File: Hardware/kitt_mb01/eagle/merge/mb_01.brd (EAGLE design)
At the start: 160 x 100 mm, 115 parts, among them CON1 ARDUINO_UNO, IC1.01 RT8293A, IC2.00 BQ24266RGET, IC3.01 LSM9DS1, P2 S2B-PH-K-S(LF)(SN), U1 MCP23017-E, U6.01 TPS61032RSARPSDO-G16, U7.01 SI1922EDH, X7.02 HEAD-LIGHT, X7.03 TAIL-LIGHT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

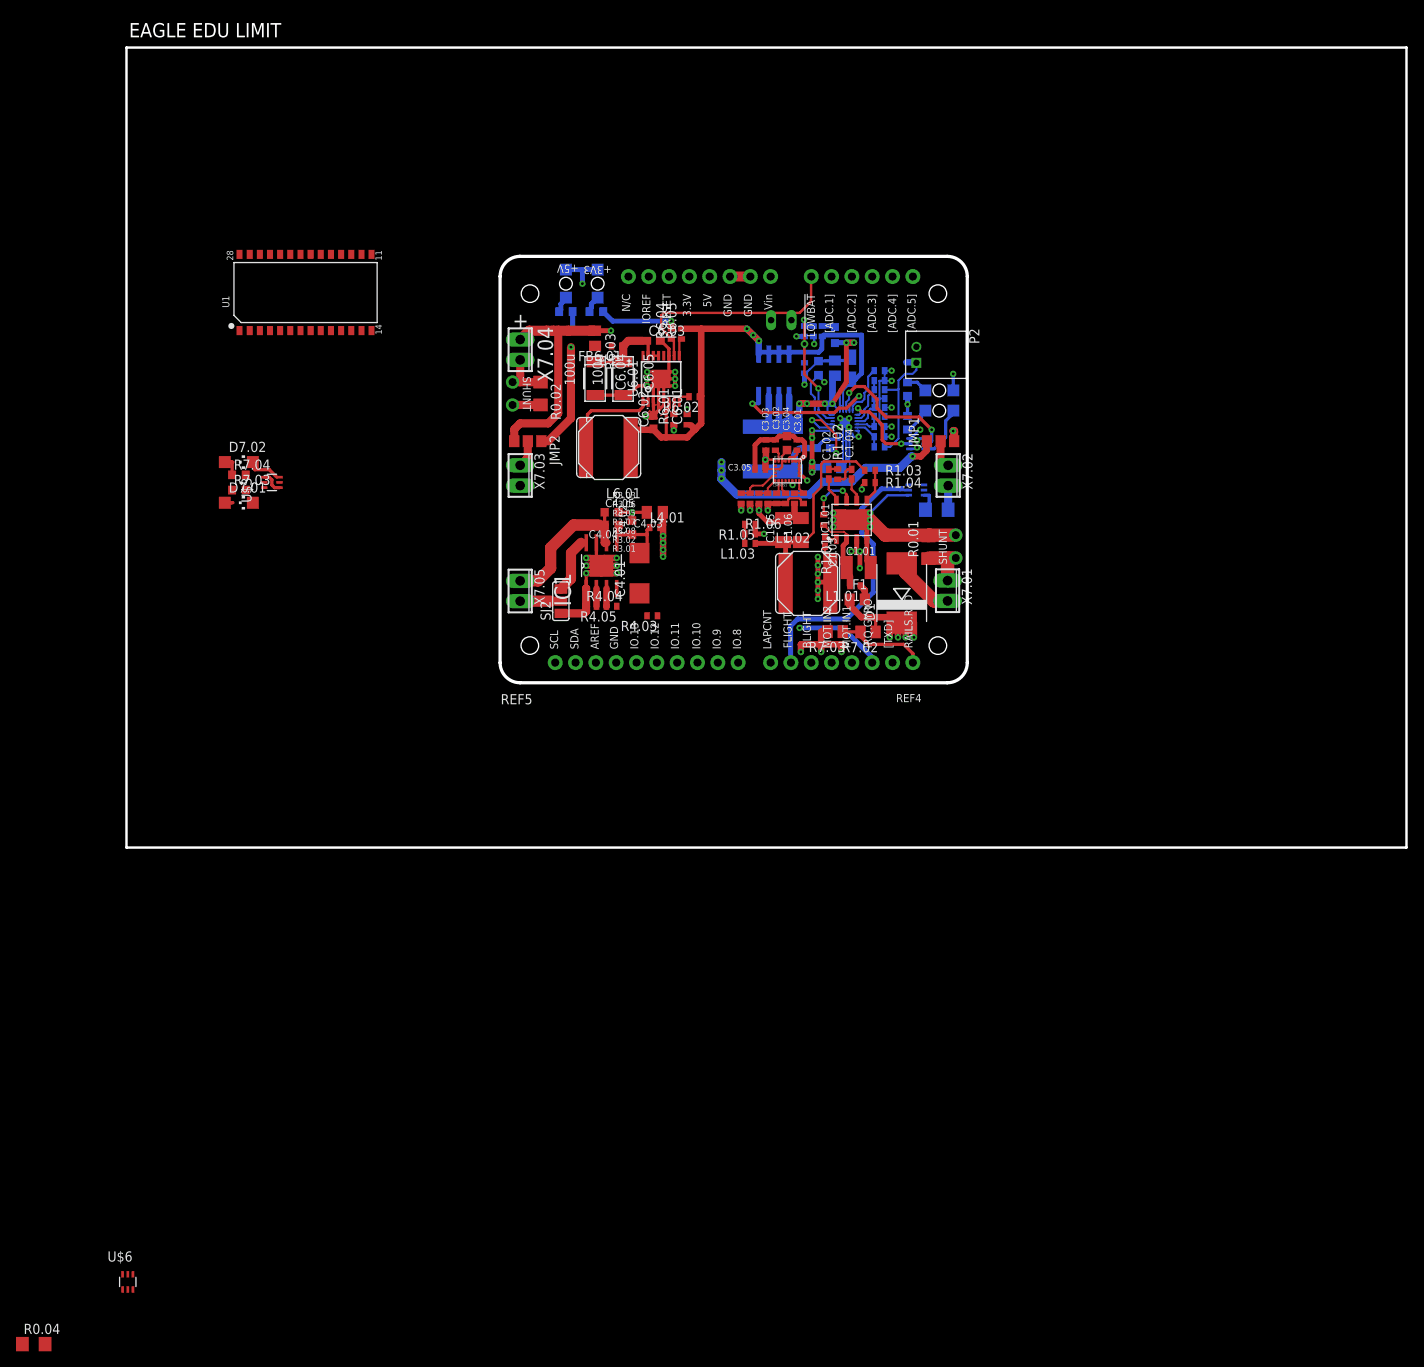
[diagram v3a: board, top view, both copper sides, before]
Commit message: snapshot of board merge : nearing it's "completion" edition
things to do:
-> either find a good placement for GP-indicators,
   or drop alltogether (what purpose?)
-> (re)move idea about port expander (DB01 maybe?)
-> add some fancy-pants logos, fiducial marks and layer count
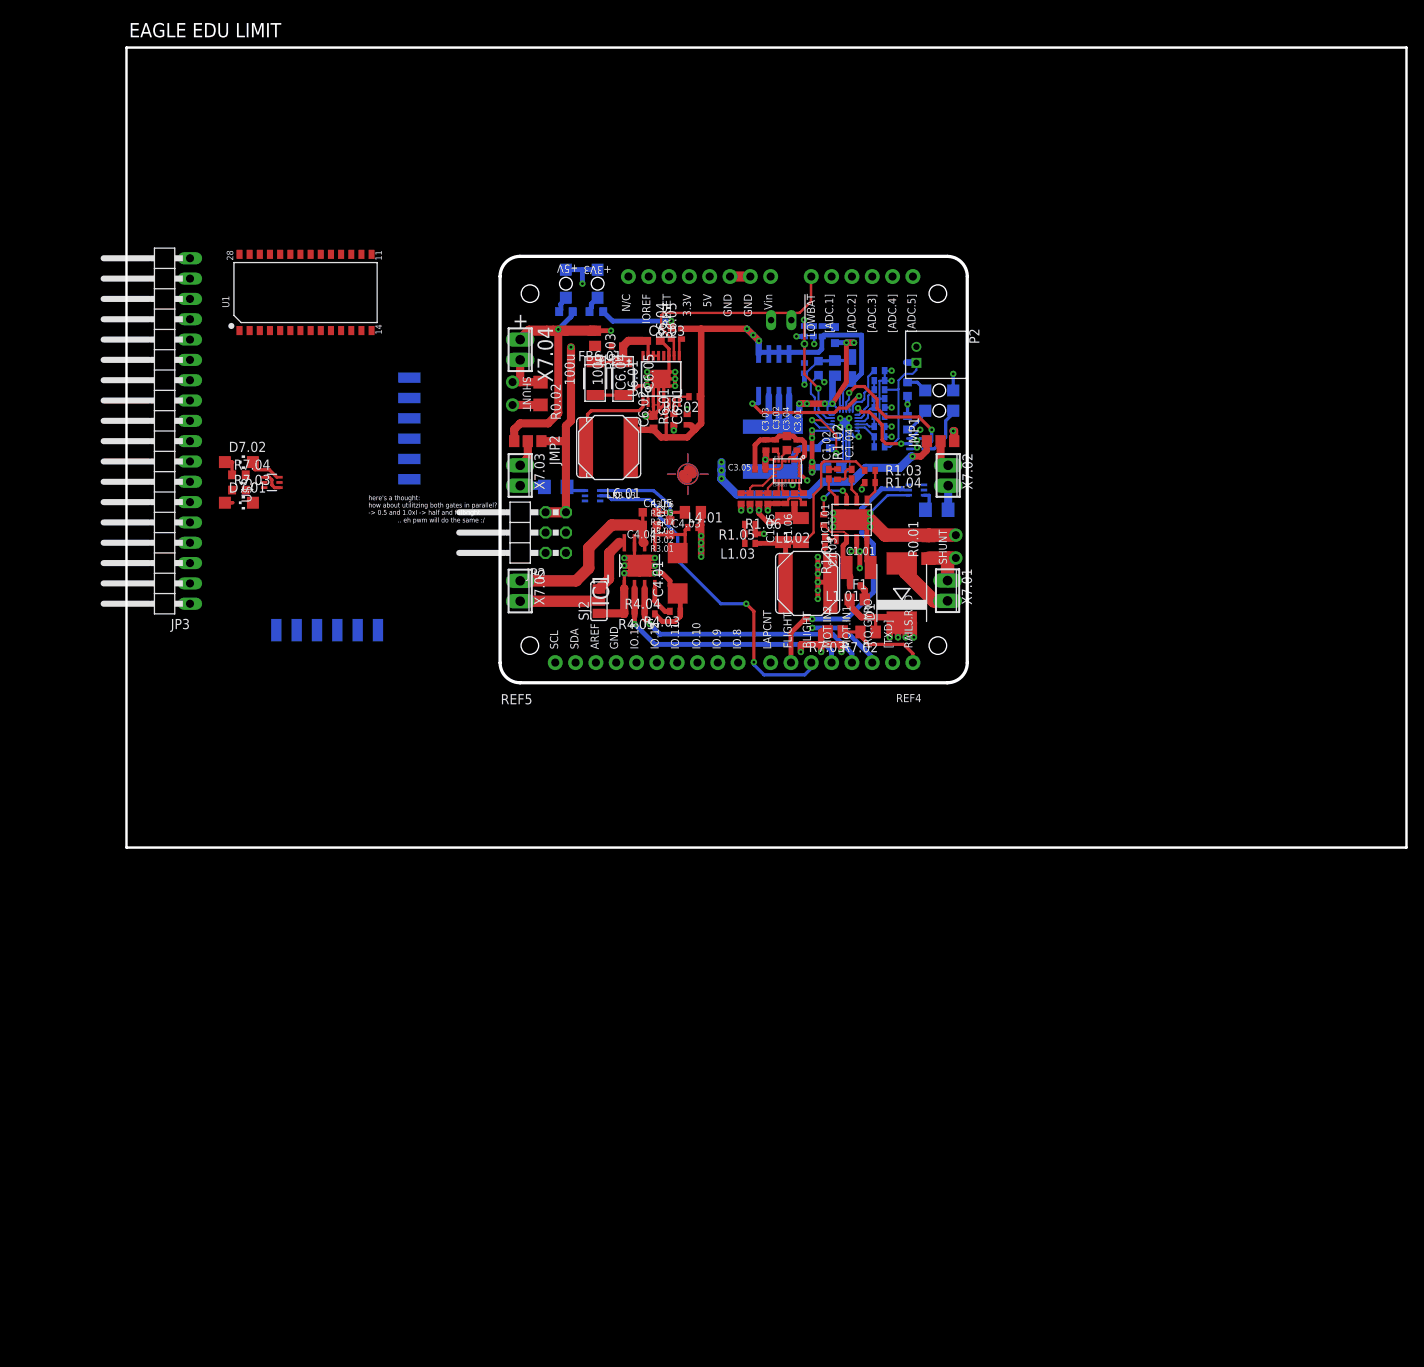
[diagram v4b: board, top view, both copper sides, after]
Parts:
- added J1, J2: CON_HEADER_1X06-SMD-RIGHT-ANGLED, dp_devices:M1X6_MALE_RIGHT_ANGLED_SMD
- added JP2: (no value), pinhead:2X03/90
- added JP3: (no value), pinhead:1X18/90
- added U$5: (no value), marks:PASS-ROUND
- moved R0.04 125.5 mm to (53.7, 45.1), flipped to the bottom
- moved U$6 114.2 mm to (58.3, 44.0), flipped to the bottom, turned to 90 degrees
- moved R4.04 4.86 mm to (62.9, 29.2)
- moved R4.05 4.86 mm to (65.4, 29.2)
- moved C4.04 4.76 mm to (65.4, 40.3)
- moved C4.05 4.76 mm to (65.4, 41.9)
- moved IC1 4.76 mm to (64.1, 35.2)
- moved SJ2 4.76 mm to (59.1, 30.8)
- moved C4.02 4.76 mm to (67.9, 40.0)
- moved C4.01 4.76 mm to (68.9, 34.3)
- moved C4.03 4.76 mm to (70.8, 41.9)
- moved L4.01 4.76 mm to (70.8, 40.0)
- moved R4.03 2.91 mm to (68.6, 29.5)
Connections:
- new net CAR.SPEED: CON1.IO.8, JP2.2
- net +3V3: now also JP2.5, JP2.6
- net CAR.BLIGHT: now also U$6.5
- net CAR.LAPCNT: now also JP2.1
- net GND: now also JP2.3, JP2.4
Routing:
- net CAR.BLIGHT: track 0.00 -> 43.0 mm, vias 0 -> 2
- net MOT.IN2: track 2.24 -> 33.8 mm, vias 0 -> 1
- net MOT.IN1: track 2.24 -> 33.6 mm, vias 0 -> 1
- net CAR.LAPCNT: track 0.00 -> 30.3 mm
- net CAR.SPEED: track 0.00 -> 29.5 mm
- net GND: track 221.4 -> 244.0 mm
- net +3V3: track 132.8 -> 145.5 mm
- net N$9: track 5.08 -> 9.84 mm
- net N$33: track 19.3 -> 24.1 mm
- net N$35: track 0.00 -> 4.00 mm
- net +12V: track 66.3 -> 62.3 mm
- net N$46: track 0.00 -> 3.09 mm
- net N$47: track 0.00 -> 2.42 mm
- net !IRQ_GYRO: track 37.2 -> 35.0 mm
- net +5V: track 139.3 -> 141.1 mm, vias 5 -> 6
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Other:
- board text added: ".. eh pwm will do the same :/"
- board text added: "here's a thought: how about utilitzing both gates in parallel? -> 0.5 and 1.0xI -> half and fulbright"

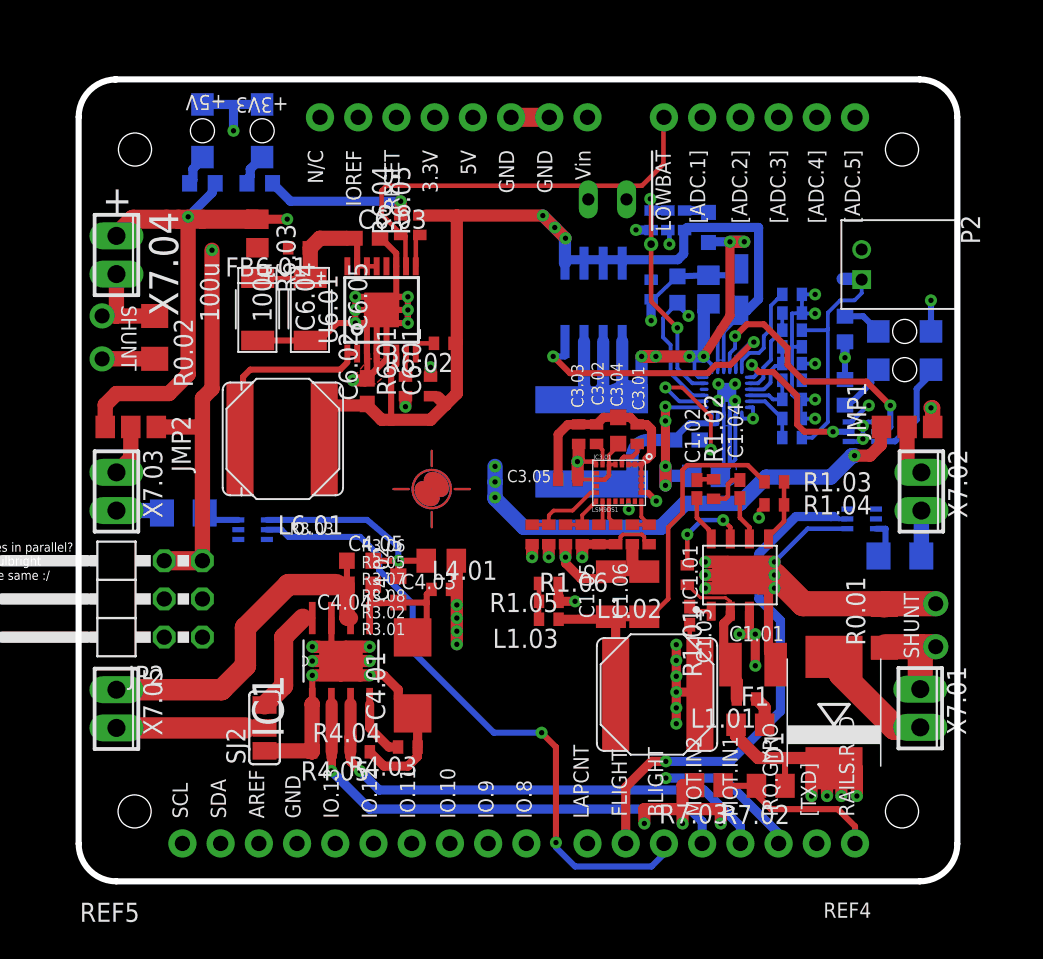
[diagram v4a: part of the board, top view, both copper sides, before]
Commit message: added layer reference onto board
for the record: it's binary, because it needs less space
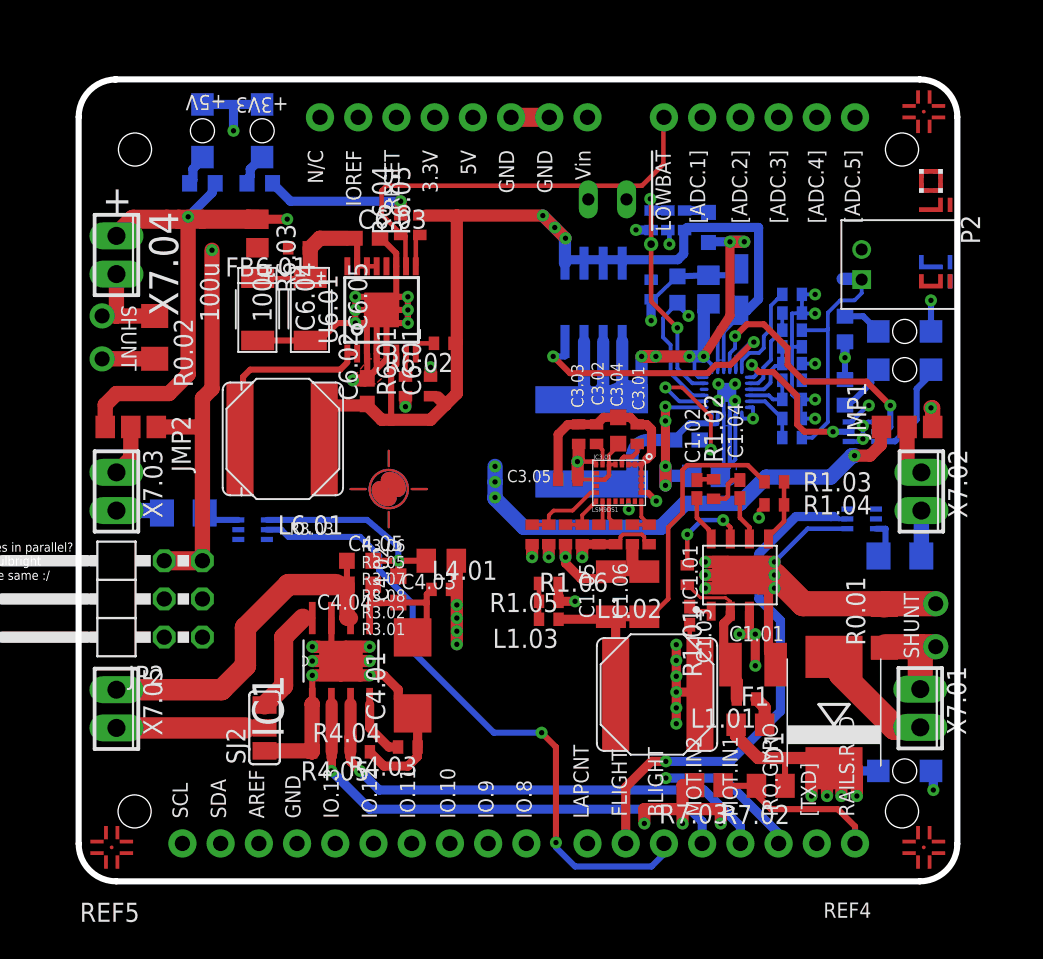
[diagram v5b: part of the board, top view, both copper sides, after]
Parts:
- added D7.07: OK+12V, led:CHIPLED_1206
- added R7,05: 330R, rcl:R0603
- added REF1: REF.LAYERS, kitt.refs:REF_LAYERS
- added U$7, U$8, U$9: (no value), marks:PASSER-CIRCLE
- moved U$5 2.86 mm to (67.3, 46.7)
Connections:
- new net N$44: D7.07.A, R7,05.1
- net +12V: now also R7,05.2
- net GND: now also D7.07.C
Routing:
- net N$49: track 0.00 -> 13.7 mm
- net N$44: track 0.00 -> 1.84 mm
- net +12V: track 62.3 -> 64.0 mm
- net GND: track 244.0 -> 245.3 mm, vias 44 -> 45
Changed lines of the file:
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@@
 <layers>
 <layer number="1" name="Top" color="4" fill="1" visible="yes" active="yes"/>
-<layer number="2" name="Route2" color="29" fill="0" visible="no" active="yes"/>
+<layer number="2" name="Route2" color="29" fill="0" visible="yes" active="yes"/>
 <layer number="3" name="Route3" color="24" fill="9" visible="yes" active="yes"/>
 <layer number="14" name="Route14" color="1" fill="6" visible="no" active="no"/>
@@
 -&gt; 0.5 and 1.0xI -&gt; half and fulbright</text>
 <text x="33.893125" y="40.64" size="0.6096" layer="46">.. eh pwm will do the same :/</text>
+<hole x="101.6" y="27.94" drill="1.6"/>
 </plain>
 <attributes>
@@
 <element name="J1" library="dp_devices" package="M1X6_MALE_RIGHT_ANGLED_SMD" value="CON_HEADER_1X06-SMD-RIGHT-ANGLED" x="32.0675" y="52.3875" rot="MR270"/>
 <element name="J2" library="dp_devices" package="M1X6_MALE_RIGHT_ANGLED_SMD" value="CON_HEADER_1X06-SMD-RIGHT-ANGLED" x="25.0825" y="30.48" rot="MR0"/>
-<element name="U$5" library="marks" package="PASS-ROUND" value="" x="70.1675" y="46.6725"/>
+<element name="U$5" library="marks" package="PASS-ROUND" value="" x="67.31" y="46.6725"/>
+<element name="R7,05" library="rcl" package="R0603" value="330R" x="97.155" y="27.94" rot="MR0"/>
+<element name="D7.07" library="led" package="CHIPLED_1206" value="OK+12V" x="101.6" y="27.94" rot="MR90"/>
+<element name="U$7" library="marks" package="PASSER-CIRCLE" value="" x="102.87" y="22.86"/>
+<element name="U$8" library="marks" package="PASSER-CIRCLE" value="" x="48.895" y="22.86"/>
+<element name="U$9" library="marks" package="PASSER-CIRCLE" value="" x="102.87" y="71.755"/>
+<element name="REF1" library="kitt.refs" package="REF_LAYERS" value="REF.LAYERS" x="102.5525" y="67.945" rot="R270"/>
 </elements>
 <signals>
@@
 <wire x1="65.86625" y1="44.62375" x2="67.945" y2="42.8625" width="0.4064" layer="16"/>
 <wire x1="67.945" y1="42.8625" x2="67.945" y2="41.91" width="0.4064" layer="16"/>
+<contactref element="D7.07" pad="C"/>
+<via x="103.505" y="26.67" extent="1-16" drill="0.35"/>
+<wire x1="103.505" y1="26.67" x2="103.505" y2="27.785" width="0.6096" layer="16"/>
+<wire x1="103.505" y1="27.785" x2="103.35" y2="27.94" width="0.6096" layer="16"/>
 <wire x1="89.349375" y1="47.550625" x2="88.9" y2="47.3225" width="0" layer="19" extent="1-16"/>
 <wire x1="19.126875" y1="44.990625" x2="48.26" y2="55.331125" width="0" layer="19" extent="1-1"/>
@@
 <wire x1="74.93" y1="30.1625" x2="79.0575" y2="27.305" width="1.27" layer="3" curve="-9.747813"/>
 <wire x1="79.0575" y1="27.305" x2="83.581875" y2="25.87625" width="1.27" layer="3" curve="42.081804"/>
+<contactref element="R7,05" pad="2"/>
+<wire x1="96.305" y1="27.94" x2="96.440625" y2="27.804375" width="0.6096" layer="16"/>
+<wire x1="96.440625" y1="27.804375" x2="96.440625" y2="26.273125" width="0.6096" layer="16"/>
 </signal>
 <signal name="RAILS.RX">
@@
 <wire x1="72.7075" y1="26.3525" x2="76.456" y2="23.12" width="1.016" layer="3" curve="-86.58744"/>
 </signal>
+<signal name="N$44">
+<contactref element="D7.07" pad="A"/>
+<contactref element="R7,05" pad="1"/>
+<wire x1="99.85" y1="27.94" x2="98.005" y2="27.94" width="0.6096" layer="16"/>
+</signal>
+<signal name="N$49">
+<wire x1="104.775" y1="68.2625" x2="102.235" y2="68.2625" width="0" layer="2"/>
+<wire x1="102.235" y1="68.2625" x2="102.235" y2="59.69" width="0" layer="2"/>
+<wire x1="102.235" y1="59.69" x2="104.775" y2="59.69" width="0" layer="2"/>
+</signal>
 </signals>
